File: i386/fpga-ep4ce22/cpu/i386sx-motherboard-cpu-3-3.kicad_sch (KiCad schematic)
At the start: 1 part, among them U1 (3/3) NG80386SX-20

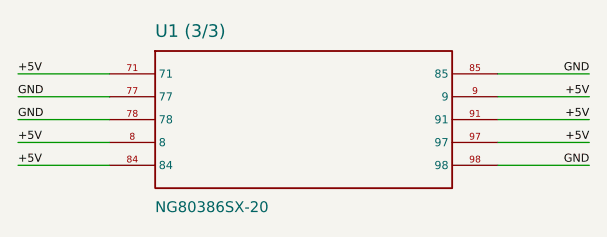
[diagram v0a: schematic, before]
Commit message: Publish the motherboards' KiCad files
From socket3@c0f6464 socket7@9205469 socket370@524f5b1 i386@bea926c
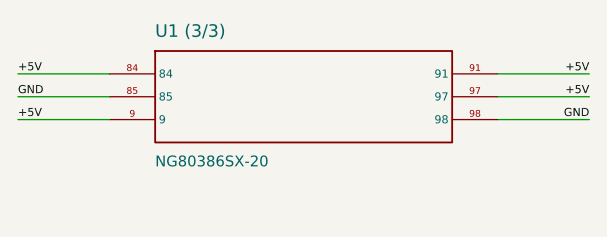
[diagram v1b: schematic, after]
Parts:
- removed U1 (3/3): NG80386SX-20, symbol gen:S5_5
- added U1 (3/3): NG80386SX-20, symbol gen:S3_3
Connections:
- net +5V: now also U1 (3/3).84, U1 (3/3).9, U1 (3/3).91, U1 (3/3).97
- net GND: now also U1 (3/3).85, U1 (3/3).98
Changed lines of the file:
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@@
     (comment 2 "Local parts are WIRED to their chip; only chip-to-chip and the rails travel by label")
   )
-  (symbol (lib_id "gen:S5_5") (at 60.96 25.40 0) (unit 1) (exclude_from_sim no) (in_bom yes) (on_board yes) (dnp no)
+  (symbol (lib_id "gen:S3_3") (at 60.96 22.86 0) (unit 1) (exclude_from_sim no) (in_bom yes) (on_board yes) (dnp no)
     (property "Reference" "U1 (3/3)" (at 44.46 16.38 0) (effects (font (size 1.4 1.4)) (justify left bottom)))
-    (property "Value" "NG80386SX-20" (at 44.46 34.42 0) (effects (font (size 1.2 1.2)) (justify left top)))
-    (instances (project "i386sx-motherboard" (path "/0ac398a9-1d89-4090-a36f-db7b4d3d6c0d/21a5e210-371b-43e6-bcae-5567ebfb9c66" (reference "U1") (unit 1))))
+    (property "Value" "NG80386SX-20" (at 44.46 29.34 0) (effects (font (size 1.2 1.2)) (justify left top)))
+    (instances (project "i386sx-motherboard" (path "/ea05416d-ce24-4c39-9113-85b33d9a88b0/16d90814-be2c-4678-adeb-7f0b87734aed" (reference "U1") (unit 1))))
   )
   (wire (pts (xy 39.38 20.32) (xy 29.22 20.32)) (stroke (width 0) (type default)))
   (wire (pts (xy 39.38 22.86) (xy 29.22 22.86)) (stroke (width 0) (type default)))
   (wire (pts (xy 39.38 25.40) (xy 29.22 25.40)) (stroke (width 0) (type default)))
-  (wire (pts (xy 39.38 27.94) (xy 29.22 27.94)) (stroke (width 0) (type default)))
-  (wire (pts (xy 39.38 30.48) (xy 29.22 30.48)) (stroke (width 0) (type default)))
   (wire (pts (xy 82.54 20.32) (xy 92.70 20.32)) (stroke (width 0) (type default)))
   (wire (pts (xy 82.54 22.86) (xy 92.70 22.86)) (stroke (width 0) (type default)))
   (wire (pts (xy 82.54 25.40) (xy 92.70 25.40)) (stroke (width 0) (type default)))
-  (wire (pts (xy 82.54 27.94) (xy 92.70 27.94)) (stroke (width 0) (type default)))
-  (wire (pts (xy 82.54 30.48) (xy 92.70 30.48)) (stroke (width 0) (type default)))
   (label "+5V" (at 29.22 20.32 0) (effects (font (size 0.9 0.9)) (justify left bottom)))
-  (label "+5V" (at 29.22 27.94 0) (effects (font (size 0.9 0.9)) (justify left bottom)))
-  (label "+5V" (at 29.22 30.48 0) (effects (font (size 0.9 0.9)) (justify left bottom)))
+  (label "+5V" (at 29.22 25.40 0) (effects (font (size 0.9 0.9)) (justify left bottom)))
+  (label "+5V" (at 92.70 20.32 0) (effects (font (size 0.9 0.9)) (justify right bottom)))
   (label "+5V" (at 92.70 22.86 0) (effects (font (size 0.9 0.9)) (justify right bottom)))
-  (label "+5V" (at 92.70 25.40 0) (effects (font (size 0.9 0.9)) (justify right bottom)))
-  (label "+5V" (at 92.70 27.94 0) (effects (font (size 0.9 0.9)) (justify right bottom)))
   (label "GND" (at 29.22 22.86 0) (effects (font (size 0.9 0.9)) (justify left bottom)))
-  (label "GND" (at 29.22 25.40 0) (effects (font (size 0.9 0.9)) (justify left bottom)))
-  (label "GND" (at 92.70 20.32 0) (effects (font (size 0.9 0.9)) (justify right bottom)))
-  (label "GND" (at 92.70 30.48 0) (effects (font (size 0.9 0.9)) (justify right bottom)))
+  (label "GND" (at 92.70 25.40 0) (effects (font (size 0.9 0.9)) (justify right bottom)))
 )
